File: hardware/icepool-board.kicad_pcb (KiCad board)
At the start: 4 copper layers, 66 x 54 mm, 180 parts, among them J1 USB Micro, J2 PWR_IN, J3 SWD, J4 I2C, J5 RS485_IN, J6 PWR_ALT, J7 SWD_ALT, J8 UART, J9 RS485_OUT, SW1 B3U-1000P, U1 ATSAMD21E, U2 ISL83488, U3 iCE40HX8K-BG121(121-Ball_caBG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, U4 iCE40HX8K-BG121(121-Ball_caBG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, U5 iCE40HX8K-BG121(121-Ball_caBG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, U6 iCE40HX8K-BG121(121-Ball_caBG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, U7 FAN2306, U8 TPS715_SC70, U9 FAN2306, X1 ASEM1-12.000MHZ, X2 ASEM1-12.000MHZ, X3 ASEM1-12.000MHZ, X4 ASEM1-12.000MHZ, Y1 16MHz

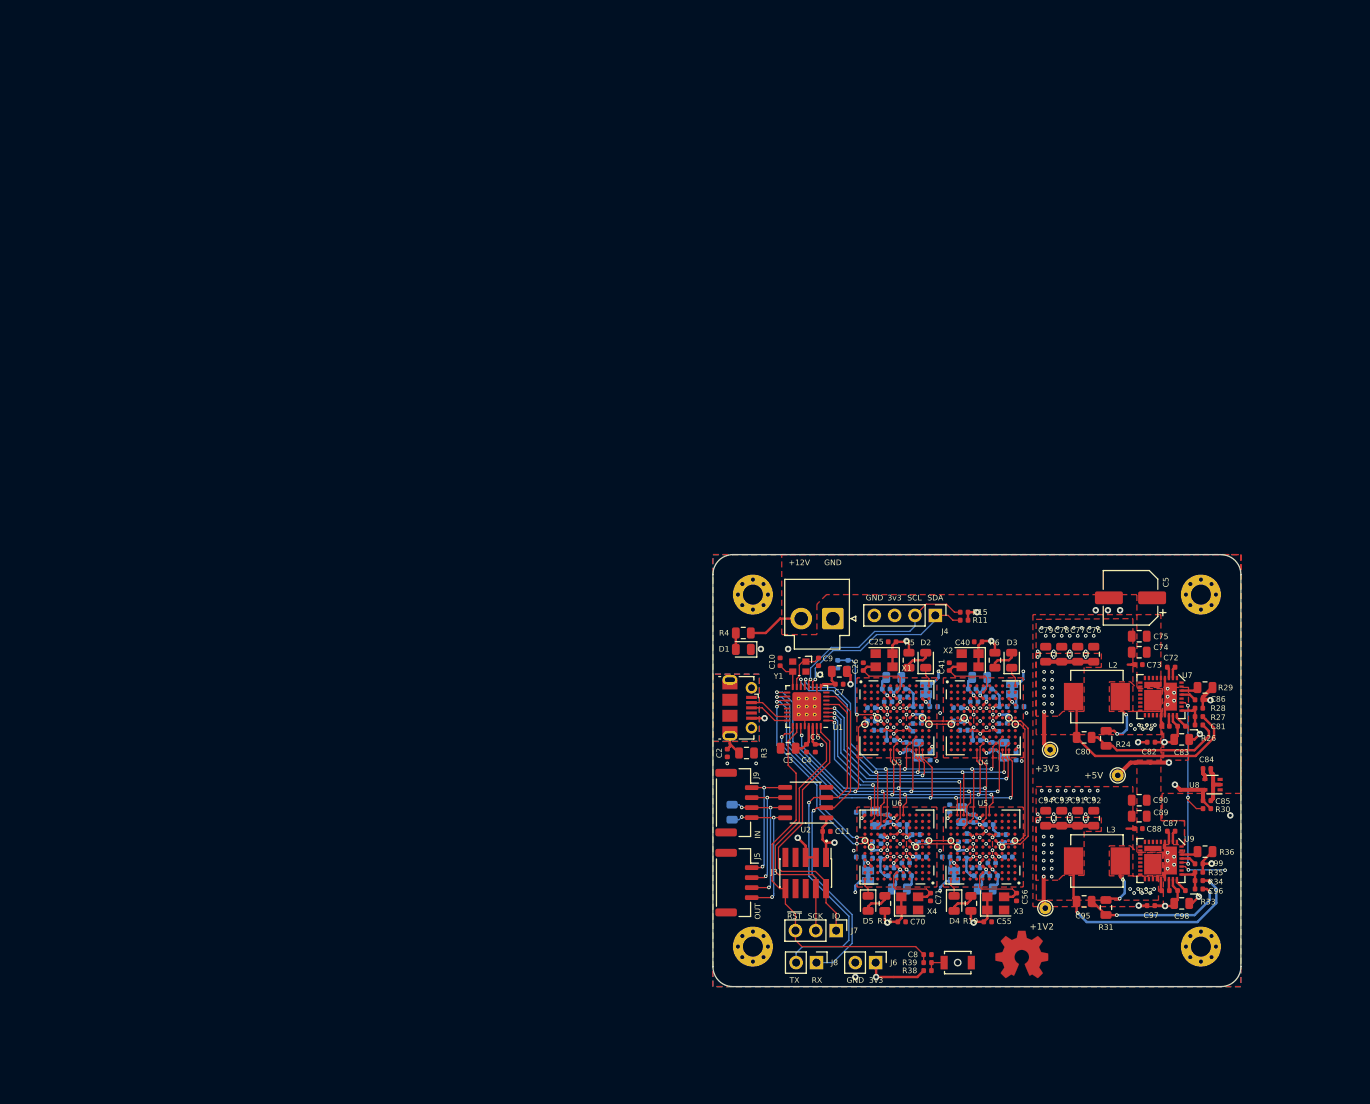
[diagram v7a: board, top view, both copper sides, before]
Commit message: Layed out passives for FGPA. Need to duplicate.
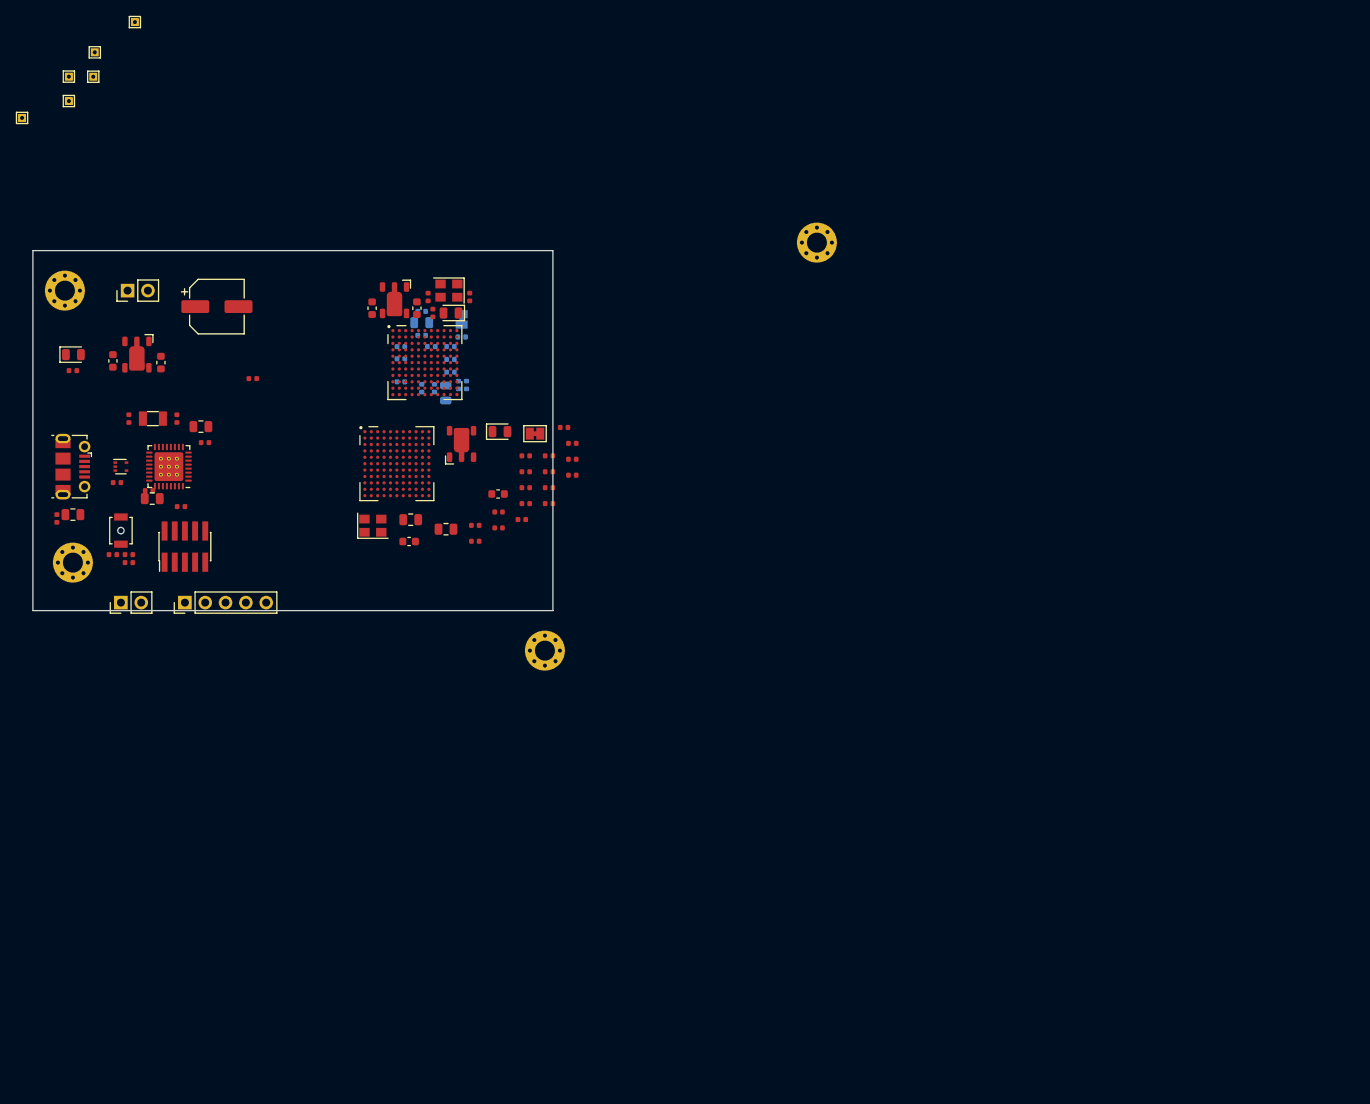
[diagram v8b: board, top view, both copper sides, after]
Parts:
- removed C100, C101, C102, C103, C17, C37, C43, C54, C57, C58, C59, C60, C61, C62, C63, C65, C66, C67, C69, C72, C73, C82, C84, C87, C88, C97: 0.1u, Capacitor_SMD:C_0402_1005Metric
- removed C23, C53, C64, C68, C74, C75, C89, C90: 10u, Capacitor_SMD:C_0805_2012Metric
- removed C55, C70: 0.01u, Capacitor_SMD:C_0402_1005Metric
- removed C56, C71: DNP, Capacitor_SMD:C_0402_1005Metric
- removed C76, C77, C78, C79, C91, C92, C93, C94: 47u, Capacitor_SMD:C_0805_2012Metric
- removed C80, C95: 1u, Capacitor_SMD:C_0805_2012Metric
- removed C81: 1n, Capacitor_SMD:C_0402_1005Metric
- removed C83, C98: 2.2u, Capacitor_SMD:C_0805_2012Metric
- removed C85: 0.47u, Capacitor_SMD:C_0402_1005Metric
- removed C86, C99: 15n, Capacitor_SMD:C_0402_1005Metric
- removed C96: 330p, Capacitor_SMD:C_0402_1005Metric
- removed D4, D5: LED_IND, LED_SMD:LED_0805_2012Metric
- removed J6: PWR_ALT, Connector_PinHeader_2.54mm:PinHeader_1x02_P2.54mm_Vertical
- removed J7: SWD_ALT, Connector_PinHeader_2.54mm:PinHeader_1x03_P2.54mm_Vertical
- removed J8: UART, Connector_PinHeader_2.54mm:PinHeader_1x02_P2.54mm_Vertical
- removed J9: RS485_OUT, Connector_JST:JST_GH_SM04B-GHS-TB_1x04-1MP_P1.25mm_Horizontal
- removed JP3, JP4: CUT_2V5, Jumper:SolderJumper-2_P1.3mm_Bridged_Pad1.0x1.5mm
- removed L2: 1u, Inductor_SMD:L_Vishay_IHLP-2525
- removed L3: 470n, Inductor_SMD:L_Vishay_IHLP-2525
- removed R12, R13, R16, R17, R20, R21: 100R, Resistor_SMD:R_0402_1005Metric
- removed R14: 1k, Resistor_SMD:R_0805_2012Metric
- removed R15, R38, R39: 4k7, Resistor_SMD:R_0402_1005Metric
- removed R24: 120R, Resistor_SMD:R_0805_2012Metric
- removed R25, R32: 1.50k, Resistor_SMD:R_0402_1005Metric
- removed R26, R33: 10R, Resistor_SMD:R_0402_1005Metric
- removed R27, R30, R34, R35: 10k, Resistor_SMD:R_0402_1005Metric
- removed R28: 2.21k, Resistor_SMD:R_0402_1005Metric
- removed R29: 56k, Resistor_SMD:R_0805_2012Metric
- removed R31: 56R, Resistor_SMD:R_0805_2012Metric
- removed R36: 20k, Resistor_SMD:R_0805_2012Metric
- removed REF**: OSHW-Symbol_6.7x6mm_Copper, Symbol:OSHW-Symbol_6.7x6mm_Copper
- removed U4: iCE40HX8K-BG121(121-Ball_caBGA), jkiv-library:BGA-121_11x11_9.0x9.0mm
- removed U7: FAN2306, jkiv-library:FAN2306
- removed X3, X4: ASEM1-12.000MHZ, Oscillator:Oscillator_SMD_Abracon_ASE-4Pin_3.2x2.5mm
- added C1: 4.7u, Capacitor_SMD:C_0603_1608Metric, F.Cu at (35.0, 61.8)
- added TP1: TestPoint, TestPoint:TestPoint_THTPad_1.0x1.0mm_Drill0.5mm, F.Cu at (29.5, 29.3)
- added TP2: TestPoint, TestPoint:TestPoint_THTPad_1.0x1.0mm_Drill0.5mm, F.Cu at (32.7, 23.2)
- added TP3: TestPoint, TestPoint:TestPoint_THTPad_1.0x1.0mm_Drill0.5mm, F.Cu at (32.5, 26.3)
- C10, C9: value 18p -> 0.1u
- C12: value 0.1u -> 22p; moved to F.Cu
- C18, C24, C44: value 0.1u -> 4.7u; footprint Capacitor_SMD:C_0402_1005Metric -> Capacitor_SMD:C_0603_1608Metric; moved to F.Cu
- C19: value 10u -> 0.1u; footprint Capacitor_SMD:C_0805_2012Metric -> Capacitor_SMD:C_0402_1005Metric
- C25: value 0.01u -> 10u; footprint Capacitor_SMD:C_0402_1005Metric -> Capacitor_SMD:C_0805_2012Metric; moved to B.Cu
- C26: value DNP -> 10u; footprint Capacitor_SMD:C_0402_1005Metric -> Capacitor_SMD:C_0805_2012Metric; moved to B.Cu
- C3: value 1u -> 47u; footprint Capacitor_SMD:C_0805_2012Metric -> Capacitor_SMD:CP_Elec_6.3x7.7
- C31, C51: value 0.1u -> 0.01u; moved to F.Cu
- C32, C52: value 0.1u -> OMIT; moved to F.Cu
- C33, C35, C36, C39, C42, C47, C48, C50, JP2, R9: moved to F.Cu
- C34, C49: value 10u -> 0.1u; footprint Capacitor_SMD:C_0805_2012Metric -> Capacitor_SMD:C_0402_1005Metric; moved to F.Cu
- C38: value 10u -> 4.7u; footprint Capacitor_SMD:C_0805_2012Metric -> Capacitor_SMD:C_0603_1608Metric; moved to F.Cu
- C4: value 0.1u -> 4.7u; footprint Capacitor_SMD:C_0402_1005Metric -> Capacitor_SMD:C_0603_1608Metric
- C40: value 0.01u -> 0.1u
- C41: value DNP -> 0.1u
- C45, C46: value 0.1u -> 10u; footprint Capacitor_SMD:C_0402_1005Metric -> Capacitor_SMD:C_0805_2012Metric; moved to F.Cu
- C5: value 47u -> 0.1u; footprint Capacitor_SMD:CP_Elec_6.3x7.7 -> Capacitor_SMD:C_0402_1005Metric
- C7: value 0.1u -> 22p
- C8: value 0.1u -> 1u; footprint Capacitor_SMD:C_0402_1005Metric -> Capacitor_SMD:C_0805_2012Metric
- D1: value 12V -> VCC
- J1: value USB Micro -> PWR_ALT; footprint Connector_USB:USB_Micro-B_Molex-105017-0001 -> Connector_PinHeader_2.54mm:PinHeader_1x02_P2.54mm_Vertical
- J2: value PWR_IN -> USB Micro; footprint Connector_JST:JST_VH_B2P-VH-B_1x02_P3.96mm_Vertical -> Connector_USB:USB_Micro-B_Molex-105017-0001
- J3: value SWD -> UART; footprint Connector_PinHeader_1.27mm:PinHeader_2x05_P1.27mm_Vertical_SMD -> Connector_PinHeader_2.54mm:PinHeader_1x02_P2.54mm_Vertical
- J4: value I2C -> SWD; footprint Connector_PinHeader_2.54mm:PinHeader_1x04_P2.54mm_Vertical -> Connector_PinHeader_1.27mm:PinHeader_2x05_P1.27mm_Vertical_SMD
- J5: value RS485_IN -> SWD_ALT; footprint Connector_JST:JST_GH_SM04B-GHS-TB_1x04-1MP_P1.25mm_Horizontal -> Connector_PinHeader_2.54mm:PinHeader_1x05_P2.54mm_Vertical
- R1: value 4k7 -> 100k; footprint Resistor_SMD:R_0402_1005Metric -> Resistor_SMD:R_0805_2012Metric; moved to F.Cu
- R10: value 1k -> 100R; footprint Resistor_SMD:R_0805_2012Metric -> Resistor_SMD:R_0402_1005Metric
- R2: value OMIT -> 0R; moved to F.Cu
- R3: value 100k -> 4k7; footprint Resistor_SMD:R_0805_2012Metric -> Resistor_SMD:R_0402_1005Metric
- R4, R5: value 1k -> 4k7; footprint Resistor_SMD:R_0805_2012Metric -> Resistor_SMD:R_0402_1005Metric
- R6: value 1k -> 100R; footprint Resistor_SMD:R_0805_2012Metric -> Resistor_SMD:R_0402_1005Metric; moved to B.Cu
- R7: value 120R -> 100R; footprint Resistor_SMD:R_0805_2012Metric -> Resistor_SMD:R_0402_1005Metric
- R8: value 100R -> 4k7; moved to F.Cu
- TP4: value 3V3 Test -> TestPoint; footprint TestPoint:TestPoint_THTPad_D1.5mm_Drill0.7mm -> TestPoint:TestPoint_THTPad_1.0x1.0mm_Drill0.5mm
- TP5: value 5V Test -> TestPoint; footprint TestPoint:TestPoint_THTPad_D1.5mm_Drill0.7mm -> TestPoint:TestPoint_THTPad_1.0x1.0mm_Drill0.5mm
- TP6: value 1V2 Test -> TestPoint; footprint TestPoint:TestPoint_THTPad_D1.5mm_Drill0.7mm -> TestPoint:TestPoint_THTPad_1.0x1.0mm_Drill0.5mm
- U1: value ATSAMD21E -> AP7361C_SOT-89-5; footprint Package_DFN_QFN:QFN-32-1EP_5x5mm_P0.5mm_EP3.6x3.6mm_ThermalVias -> jkiv-library:SOT89-5
- U2: value ISL83488 -> TPD3E001DRLR; footprint Package_SO:SO-8_3.9x4.9mm_P1.27mm -> Package_TO_SOT_SMD:SOT-553
- U3: value iCE40HX8K-BG121(121-Ball_caBGA) -> ATSAMD21E; footprint jkiv-library:BGA-121_11x11_9.0x9.0mm -> Package_DFN_QFN:QFN-32-1EP_5x5mm_P0.5mm_EP3.6x3.6mm_ThermalVias
- U5: value iCE40HX8K-BG121(121-Ball_caBGA) -> AP7361C_SOT-89-5; footprint jkiv-library:BGA-121_11x11_9.0x9.0mm -> jkiv-library:SOT89-5
- U8: value TPS715_SC70 -> AP7361C_SOT-89-5; footprint Package_TO_SOT_SMD:SOT-353_SC-70-5 -> jkiv-library:SOT89-5
- U9: value FAN2306 -> iCE40HX8K-BG121(121-Ball_caBGA); footprint jkiv-library:FAN2306 -> jkiv-library:BGA-121_11x11_9.0x9.0mm
- Y1: value 16MHz -> ABS07-32.768KHZ; footprint Crystal:Crystal_SMD_Abracon_ABM10-4Pin_2.5x2.0mm -> Crystal:Crystal_SMD_3215-2Pin_3.2x1.5mm
- moved TP6 161.6 mm to (23.6, 31.4)
- moved TP5 157.5 mm to (29.5, 26.3)
- moved TP4 146.2 mm to (37.7, 19.4)
- moved H4 141.1 mm to (30.0, 87.0)
- moved C5 127.5 mm to (35.5, 77.0), turned to 0 degrees
- moved SW1 117.7 mm to (36.0, 83.0), turned to 90 degrees
- moved C8 112.4 mm to (39.9, 79.0)
- moved U9 107.6 mm to (70.5, 74.6), turned to 0 degrees
- moved C12 104.9 mm to (37.0, 69.0), turned to 90 degrees
- moved U8 103.1 mm to (78.6, 72.2), turned to 0 degrees
- moved U5 100.4 mm to (70.2, 54.2)
- moved R1 98.7 mm to (30.0, 81.0), turned to 0 degrees
- moved R5 98.3 mm to (37.0, 87.0), turned to 0 degrees
- moved J2 96.9 mm to (30.0, 75.0), turned to 270 degrees
- moved R3 96.8 mm to (30.0, 63.0)
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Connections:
- C10 pad 1: /XOUT -> GND
- C10 pad 2: GND -> +3V3
- C11 pad 1: +3V3 -> GND
- C11 pad 2: GND -> /VDDANA
- C12 pad 1: GND -> /XOUT
- C12 pad 2: +1V2 -> GND
- C13 pad 2: +3V3 -> /ICE40HX8K-BG121_0/VCC0
- C14 pad 2: +3V3 -> /ICE40HX8K-BG121_0/VCC0
- C15 pad 2: +1V2 -> /ICE40HX8K-BG121_0/VCC0
- C16 pad 2: +3V3 -> /ICE40HX8K-BG121_0/VCC0
- C18 pad 1: GND -> VCC
- C18 pad 2: +3V3 -> GND
- C19 pad 1: /ICE40HX8K-BG121_0/VCCPLL0 -> GND
- C19 pad 2: /ICE40HX8K-BG121_0/GNDPLL0 -> +3V3
- C20 pad 1: /ICE40HX8K-BG121_0/VCCPLL0 -> GND
- C20 pad 2: /ICE40HX8K-BG121_0/GNDPLL0 -> +3V3
- C21 pad 2: +1V2 -> +3V3
- C24 pad 1: /ICE40HX8K-BG121_0/VCCPLL1 -> /ICE40HX8K-BG121_0/VCC0
- C24 pad 2: /ICE40HX8K-BG121_0/GNDPLL1 -> GND
- C25 pad 1: GND -> /ICE40HX8K-BG121_0/VCCPLL0
- C25 pad 2: +3V3 -> /ICE40HX8K-BG121_0/GNDPLL0
- C26 pad 1: GND -> /ICE40HX8K-BG121_0/VCCPLL1
- C26 pad 2: /ICE40HX8K-BG121_0/CLK -> /ICE40HX8K-BG121_0/GNDPLL1
- C27 pad 2: +1V2 -> +3V3
- C28 pad 2: +3V3 -> /ICE40HX8K-BG121_0/VPP_2V5
- C29 pad 1: GND -> /ICE40HX8K-BG121_0/VCCPLL0
- C29 pad 2: +3V3 -> /ICE40HX8K-BG121_0/GNDPLL0
- C3 pad 1: GND -> VCC
- C3 pad 2: /VDDCORE -> GND
- C30 pad 1: GND -> /ICE40HX8K-BG121_0/VCCPLL1
- C30 pad 2: +1V2 -> /ICE40HX8K-BG121_0/GNDPLL1
- C32 pad 2: +1V2 -> /ICE40HX8K-BG121_0/CLK
- C33 pad 2: +3V3 -> /ICE40HX8K-BG121_1/VCC0
- C34 pad 1: /ICE40HX8K-BG121_1/VCCPLL0 -> GND
- C34 pad 2: /ICE40HX8K-BG121_1/GNDPLL0 -> /ICE40HX8K-BG121_1/VCC0
- C35 pad 1: /ICE40HX8K-BG121_1/VCCPLL0 -> GND
- C35 pad 2: /ICE40HX8K-BG121_1/GNDPLL0 -> /ICE40HX8K-BG121_1/VCC0
- C36 pad 2: +1V2 -> /ICE40HX8K-BG121_1/VCC0
- C38 pad 1: /ICE40HX8K-BG121_1/VCCPLL1 -> VCC
- C38 pad 2: /ICE40HX8K-BG121_1/GNDPLL1 -> GND
- C39 pad 1: /ICE40HX8K-BG121_1/VCCPLL1 -> GND
- C39 pad 2: /ICE40HX8K-BG121_1/GNDPLL1 -> +3V3
- C4 pad 1: GND -> +3V3
- C4 pad 2: /VDDCORE -> GND
- C41 pad 2: /ICE40HX8K-BG121_1/CLK -> +3V3
- C42 pad 2: +1V2 -> +3V3
- C44 pad 1: GND -> /ICE40HX8K-BG121_1/VCC0
- C44 pad 2: +3V3 -> GND
- C45 pad 1: GND -> /ICE40HX8K-BG121_1/VCCPLL0
- C45 pad 2: +1V2 -> /ICE40HX8K-BG121_1/GNDPLL0
- C46 pad 1: GND -> /ICE40HX8K-BG121_1/VCCPLL1
- C46 pad 2: +3V3 -> /ICE40HX8K-BG121_1/GNDPLL1
- C47 pad 2: +1V2 -> +3V3
- C48 pad 2: +3V3 -> /ICE40HX8K-BG121_1/VPP_2V5
- C49 pad 1: /ICE40HX8K-BG121_2/VCCPLL0 -> /ICE40HX8K-BG121_1/VCCPLL0
- C49 pad 2: /ICE40HX8K-BG121_2/GNDPLL0 -> /ICE40HX8K-BG121_1/GNDPLL0
- C50 pad 1: /ICE40HX8K-BG121_2/VCCPLL0 -> /ICE40HX8K-BG121_1/VCCPLL1
- C50 pad 2: /ICE40HX8K-BG121_2/GNDPLL0 -> /ICE40HX8K-BG121_1/GNDPLL1
- C51 pad 2: +1V2 -> +3V3
- C52 pad 2: +3V3 -> /ICE40HX8K-BG121_1/CLK
- C6 pad 1: GND -> /~RESET
- C6 pad 2: +3V3 -> GND
- C7 pad 1: GND -> /XIN
- C7 pad 2: /VDDANA -> GND
- C8 pad 1: /~RESET -> GND
- C8 pad 2: GND -> /VDDCORE
- C9 pad 1: /XIN -> GND
- C9 pad 2: GND -> /VDDCORE
- J1 pad 1: Net-(J1-Pad1) -> GND
- J1 pad 2: /USB_D- -> VCC
- J2 pad 1: GND -> VCC
- J2 pad 2: VCC -> /USB_D-
- J3 pad 1: +3V3 -> /RX
- J3 pad 2: /SWD_IO -> /TX
- J4 pad 1: /I2C_SDA -> +3V3
- J4 pad 2: /I2C_SCL -> /SWD_IO
- J4 pad 3: +3V3 -> GND
- J4 pad 4: GND -> /SWD_CLK
- J5 pad 1: /TX- -> +3V3
- J5 pad 2: /TX+ -> GND
- J5 pad 3: /RX- -> /SWD_IO
- J5 pad 4: /RX+ -> /SWD_CLK
- R1 pad 1: +3V3 -> /USB_SHIELD
- R1 pad 2: /READY_0 -> GND
- R10 pad 1: Net-(D4-Pad2) -> /ICE40HX8K-BG121_1/VCCPLL1
- R10 pad 2: +3V3 -> +1V2
- R11 pad 1: +3V3 -> Net-(D3-Pad2)
- R11 pad 2: /I2C_SDA -> +3V3
- R3 pad 1: /USB_SHIELD -> VCC
- R3 pad 2: GND -> Net-(D1-Pad2)
- R4 pad 1: VCC -> Net-(R4-Pad1)
- R4 pad 2: Net-(D1-Pad2) -> /~RESET
- R5 pad 1: Net-(D2-Pad2) -> +3V3
- R5 pad 2: +3V3 -> Net-(R4-Pad1)
- R6 pad 1: Net-(D3-Pad2) -> /ICE40HX8K-BG121_0/VCCPLL0
- R6 pad 2: +3V3 -> +1V2
- R7 pad 1: /RX- -> /ICE40HX8K-BG121_0/VCCPLL1
- R7 pad 2: /RX+ -> +1V2
- R8 pad 1: /ICE40HX8K-BG121_0/VCCPLL0 -> Net-(D2-Pad2)
- R8 pad 2: +1V2 -> +3V3
- R9 pad 1: /ICE40HX8K-BG121_0/VCCPLL1 -> /ICE40HX8K-BG121_1/VCCPLL0
- SW1 pad 1: Net-(R38-Pad2) -> Net-(R4-Pad1)
- TP4 pad 1: +3V3 -> /MOSI
- TP5 pad 1: +5V -> /FIFO_0_1
- TP6 pad 1: +1V2 -> /MISO
- U1 pad 1: /SPI_SS_B_3 -> VCC
- U1 pad 2: /SPI_SS_B_2 -> GND
- U1 pad 3: /SPI_SS_B_1 -> (no net)
- U1 pad 4: /SPI_SS_B_0 -> VCC
- U1 pad 5: /TX -> +3V3
- U2 pad 1: +3V3 -> /USB_D-
- U2 pad 2: /RX -> /USB_D+
- U2 pad 3: /TX -> GND
- U2 pad 4: GND -> (no net)
- U2 pad 5: /TX- -> VCC
- U6 pad A1: Net-(U6-PadA1) -> (no net)
- U6 pad A10: Net-(U6-PadA10) -> (no net)
- U6 pad A11: /ICE40HX8K-BG121_3/LED_IND -> /ICE40HX8K-BG121_0/LED_IND
- U6 pad A2: Net-(U6-PadA2) -> (no net)
- U6 pad A3: Net-(U6-PadA3) -> (no net)
- U6 pad A4: Net-(U6-PadA4) -> (no net)
- U6 pad A5: Net-(U6-PadA5) -> (no net)
- U6 pad A6: Net-(U6-PadA6) -> (no net)
- U6 pad A7: Net-(U6-PadA7) -> (no net)
- U6 pad A8: Net-(U6-PadA8) -> (no net)
- U6 pad A9: Net-(U6-PadA9) -> (no net)
- U6 pad B1: Net-(U6-PadB1) -> (no net)
- U6 pad B10: Net-(U6-PadB10) -> (no net)
- U6 pad B11: Net-(U6-PadB11) -> (no net)
- U6 pad B2: Net-(U6-PadB2) -> (no net)
- U6 pad B3: Net-(U6-PadB3) -> (no net)
- U6 pad B4: Net-(U6-PadB4) -> (no net)
- U6 pad B5: Net-(U6-PadB5) -> (no net)
- U6 pad B6: /ICE40HX8K-BG121_3/CLK -> /ICE40HX8K-BG121_0/CLK
- U6 pad B7: Net-(U6-PadB7) -> (no net)
- U6 pad B8: Net-(U6-PadB8) -> (no net)
- U6 pad B9: Net-(U6-PadB9) -> (no net)
- U6 pad C1: Net-(U6-PadC1) -> (no net)
- U6 pad C10: /ICE40HX8K-BG121_3/VPP_2V5 -> /ICE40HX8K-BG121_0/VPP_2V5
- U6 pad C11: Net-(U6-PadC11) -> (no net)
- U6 pad C2: Net-(U6-PadC2) -> (no net)
- U6 pad C3: Net-(U6-PadC3) -> (no net)
- U6 pad C4: Net-(U6-PadC4) -> (no net)
- U6 pad C5: /ICE40HX8K-BG121_3/GNDPLL1 -> /ICE40HX8K-BG121_0/GNDPLL1
- U6 pad C6: /ICE40HX8K-BG121_3/VCCPLL1 -> /ICE40HX8K-BG121_0/VCCPLL1
- U6 pad C7: Net-(U6-PadC7) -> (no net)
- U6 pad C8: Net-(U6-PadC8) -> (no net)
- U6 pad C9: Net-(U6-PadC9) -> (no net)
- U6 pad D1: Net-(U6-PadD1) -> (no net)
- U6 pad D10: Net-(U6-PadD10) -> (no net)
- U6 pad D11: Net-(U6-PadD11) -> (no net)
- U6 pad D2: Net-(U6-PadD2) -> (no net)
- U6 pad D3: Net-(U6-PadD3) -> (no net)
- U6 pad D4: +1V2 -> /ICE40HX8K-BG121_0/VCC0
- U6 pad D5: Net-(U6-PadD5) -> (no net)
- U6 pad D7: Net-(U6-PadD7) -> (no net)
- U6 pad D8: +1V2 -> /ICE40HX8K-BG121_0/VCC0
- U6 pad D9: Net-(U6-PadD9) -> (no net)
- U6 pad E1: Net-(U6-PadE1) -> (no net)
- U6 pad E10: Net-(U6-PadE10) -> (no net)
- U6 pad E11: Net-(U6-PadE11) -> (no net)
- U6 pad E2: Net-(U6-PadE2) -> (no net)
- U6 pad E3: Net-(U6-PadE3) -> (no net)
- U6 pad E8: Net-(U6-PadE8) -> (no net)
- U6 pad E9: Net-(U6-PadE9) -> (no net)
- U6 pad F1: Net-(U6-PadF1) -> (no net)
- U6 pad F10: /READY -> /READY_0_1
- U6 pad F11: Net-(U6-PadF11) -> (no net)
- U6 pad F2: Net-(U6-PadF2) -> (no net)
- U6 pad F3: /READY_2_3 -> /READY_0
- U6 pad F4: Net-(U6-PadF4) -> (no net)
- U6 pad F9: Net-(U6-PadF9) -> (no net)
- U6 pad G1: /FIFO_2_3 -> /MOSI
- U6 pad G10: Net-(U6-PadG10) -> (no net)
- U6 pad G11: /MISO -> /FIFO_0_1
- U6 pad G2: Net-(U6-PadG2) -> (no net)
- U6 pad G3: Net-(U6-PadG3) -> (no net)
- U6 pad G8: Net-(U6-PadG8) -> (no net)
- U6 pad G9: Net-(U6-PadG9) -> (no net)
- U6 pad H1: Net-(U6-PadH1) -> (no net)
- U6 pad H10: Net-(U6-PadH10) -> (no net)
- U6 pad H11: Net-(U6-PadH11) -> (no net)
- U6 pad H2: Net-(U6-PadH2) -> (no net)
- U6 pad H3: Net-(U6-PadH3) -> (no net)
- U6 pad H4: +1V2 -> /ICE40HX8K-BG121_0/VCC0
- U6 pad H7: Net-(U6-PadH7) -> (no net)
- U6 pad H8: +1V2 -> /ICE40HX8K-BG121_0/VCC0
- U6 pad H9: Net-(U6-PadH9) -> (no net)
- U6 pad J1: Net-(U6-PadJ1) -> (no net)
- U6 pad J10: Net-(U6-PadJ10) -> (no net)
- U6 pad J11: Net-(U6-PadJ11) -> (no net)
- U6 pad J2: Net-(U6-PadJ2) -> (no net)
- U6 pad J3: Net-(U6-PadJ3) -> (no net)
- U6 pad J4: Net-(U6-PadJ4) -> (no net)
- U6 pad J5: Net-(U6-PadJ5) -> (no net)
- U6 pad J6: /ICE40HX8K-BG121_3/VCCPLL0 -> /ICE40HX8K-BG121_0/VCCPLL0
- U6 pad J7: Net-(U6-PadJ7) -> (no net)
- U6 pad J8: Net-(U6-PadJ8) -> (no net)
- U6 pad K1: Net-(U6-PadK1) -> (no net)
- U6 pad K10: /SPI_SS_B_3 -> /SPI_SS_B_0
- U6 pad K11: Net-(U6-PadK11) -> (no net)
- U6 pad K2: Net-(U6-PadK2) -> (no net)
- U6 pad K3: Net-(U6-PadK3) -> (no net)
- U6 pad K4: Net-(U6-PadK4) -> (no net)
- U6 pad K5: Net-(U6-PadK5) -> (no net)
- U6 pad K6: /~GS -> /~SSEL
- U6 pad K7: Net-(U6-PadK7) -> (no net)
- U6 pad K8: /CDONE -> /CDONE_0
- U6 pad K9: /ICE40HX8K-BG121_3/GMISO -> (no net)
- U6 pad L1: Net-(U6-PadL1) -> (no net)
- U6 pad L2: Net-(U6-PadL2) -> (no net)
- U6 pad L3: Net-(U6-PadL3) -> (no net)
- U6 pad L4: Net-(U6-PadL4) -> (no net)
- U6 pad L6: /ICE40HX8K-BG121_3/GNDPLL0 -> /ICE40HX8K-BG121_0/GNDPLL0
- U6 pad L7: Net-(U6-PadL7) -> (no net)
- U6 pad L8: Net-(U6-PadL8) -> (no net)
- U6 pad L9: /CRESET_B -> /CRESET_B_0
- U8 pad 1: Net-(U8-Pad1) -> VCC
- U8 pad 3: Net-(U8-Pad3) -> (no net)
- U8 pad 5: +5V -> /ICE40HX8K-BG121_1/VCC0
- Y1 pad 2: GND -> /XOUT
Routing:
- net +3V3: track 196.8 -> 0.00 mm, vias 53 -> 0
- net +1V2: track 81.1 -> 0.00 mm, vias 34 -> 0
- net /MOSI: track 70.1 -> 0.00 mm, vias 6 -> 0
- net +5V: track 66.4 -> 0.00 mm, vias 6 -> 0
- net /SCK: track 55.5 -> 0.00 mm, vias 5 -> 0
- net /~WE: track 53.3 -> 0.00 mm, vias 5 -> 0
- net /CDONE: track 52.5 -> 0.00 mm, vias 5 -> 0
- net /CRESET_B: track 51.2 -> 0.00 mm, vias 5 -> 0
- net /~GS: track 48.7 -> 0.00 mm, vias 3 -> 0
- net /~RESET: track 48.3 -> 0.00 mm
- net /TX: track 45.8 -> 0.00 mm, vias 1 -> 0
- net GND: track 45.0 -> 0.00 mm, vias 114 -> 0
- net /RX: track 43.6 -> 0.00 mm, vias 1 -> 0
- net /SWD_IO: track 34.1 -> 0.00 mm
- net /SWD_CLK: track 33.3 -> 0.00 mm
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- removed copper zone on F.Cu, net +1V2
- removed copper zone on In1.Cu, net +1V2
- removed copper zone on F.Cu, net +3V3
- removed copper zone on In1.Cu, net +3V3
- removed copper zone on F.Cu, net /Power/SW_1v2
- removed copper zone on F.Cu, net /Power/SW_3v3
- removed copper zone on B.Cu, net /USB_SHIELD
- removed copper zone on F.Cu, net /USB_SHIELD
- removed copper zone on In1.Cu, net /USB_SHIELD
- removed copper zone on In2.Cu, net /USB_SHIELD
- removed copper zone on B.Cu, net GND
- removed copper zone on F.Cu, net GND
- removed copper zone on In1.Cu, net GND
- removed copper zone on In2.Cu, net GND
- removed copper zone on F.Cu, net VCC
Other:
- board size 66 x 54 mm -> 65 x 45 mm
- board text removed: "+12V"
- board text removed: "+1V2"
- board text removed: "+3V3"
- board text removed: "+5V"
- board text removed: "3v3"
- board text removed: "GND"
- board text removed: "HI"
- board text removed: "IN"
- board text removed: "IO"
- board text removed: "LO"
- board text removed: "OUT"
- board text removed: "READY"
- board text removed: "RS485 Term."
- board text removed: "RX"
- board text removed: "SCK"
- board text removed: "SCL"
- board text removed: "SDA"
- board text removed: "TX"
- board text removed: "icepool 2020-02 fourside.io"
- board text removed: "~RST"
